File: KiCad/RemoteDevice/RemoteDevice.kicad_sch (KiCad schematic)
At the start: 56 parts, among them J1 pin, J2 pin, Q1 PJA3411, Q2 PJA3411, SW1 BP, SW2 BP, U1 XC9140, U10 XBEE-3, U2 STM32L041F6Px, U3 MCP6281, U4 ADT7410TRZ, U5 MCP6281, U6 RT606, U7 Microphone, U8 LD2981CU33, U9 Con_4pts

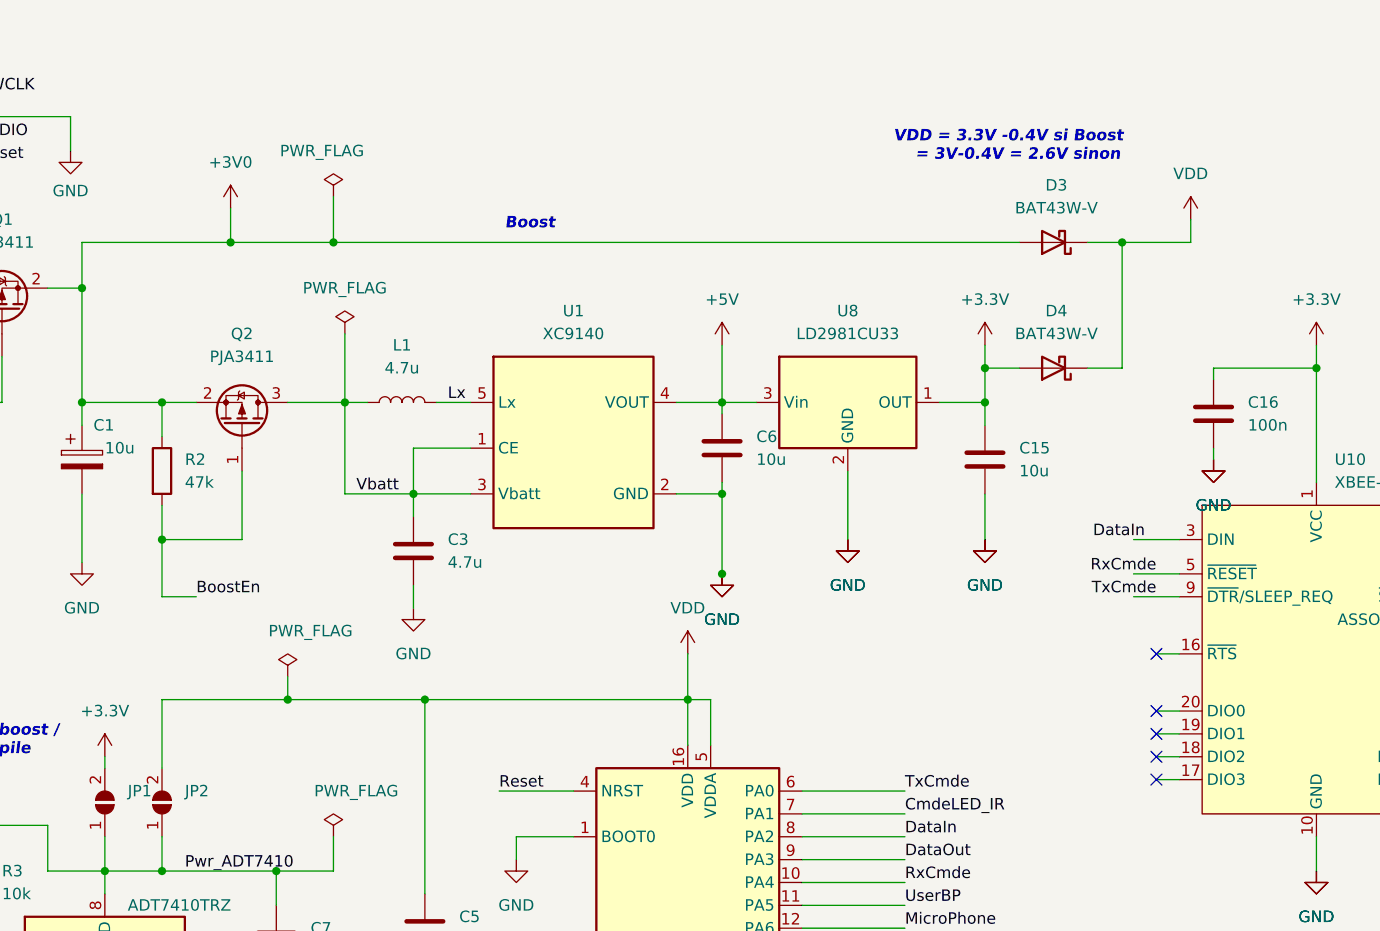
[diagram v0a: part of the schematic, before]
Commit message: Version modifié : ajout pull up RT606 pour adapt niveau, supression BAT43, ajout capa de découplage uC. A tester
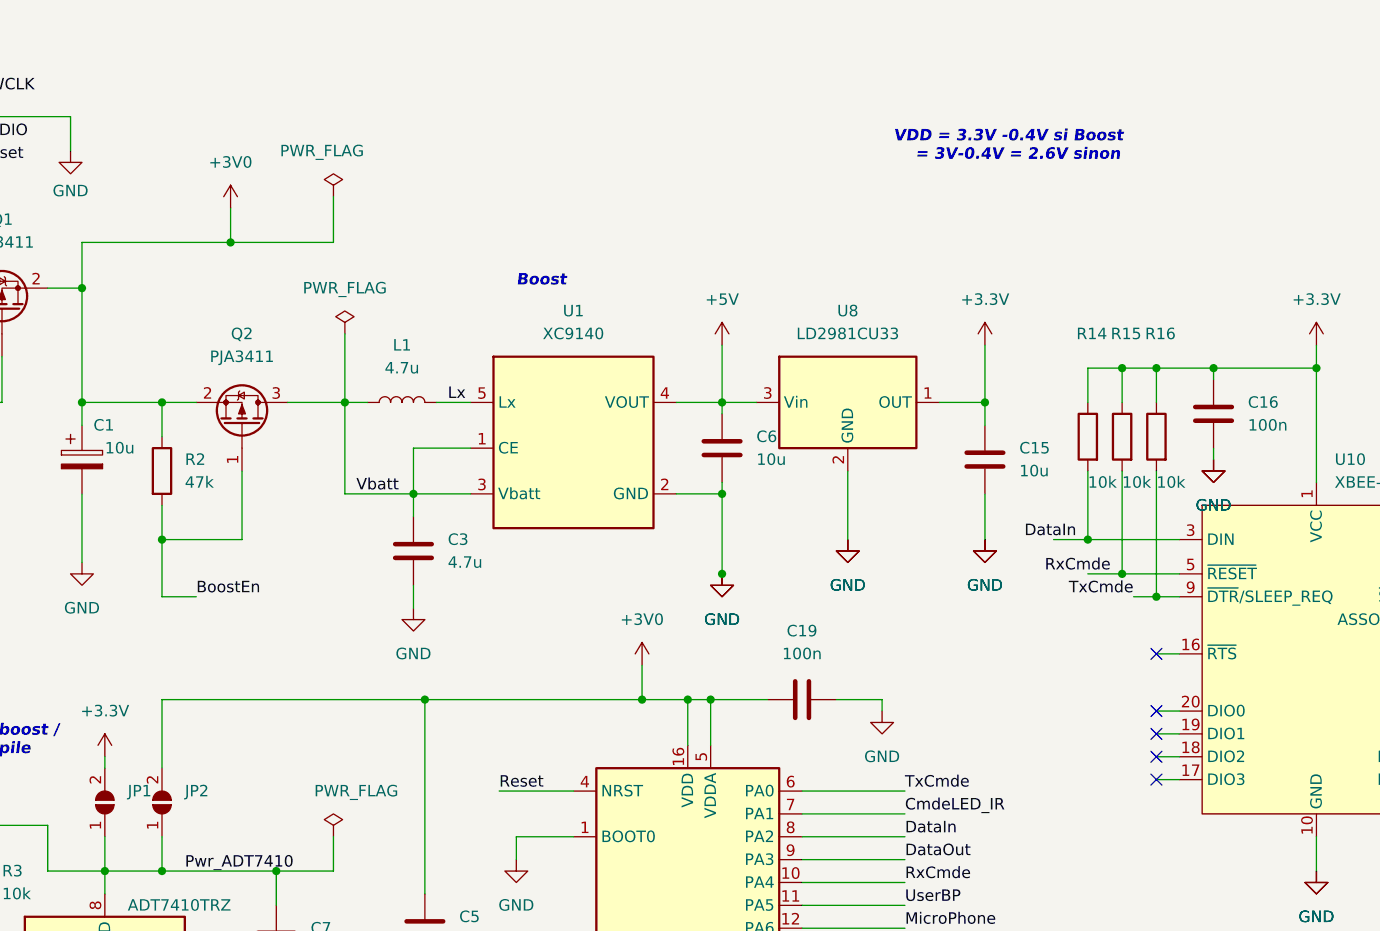
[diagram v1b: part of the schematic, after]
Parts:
- removed D3, D4: BAT43W-V, Diode_SMD:D_SOD-123, symbol Diode:BAT43W-V
- added C19: 100n, Capacitor_SMD:C_1206_3216Metric, symbol Device:C
- added R14, R15, R16: 10k, Resistor_SMD:R_1206_3216Metric, symbol Device:R
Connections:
- net VDD is gone; now on net +3V0: C5.1, JP2.2 (B), U2.16 (VDD), U2.5 (VDDA)
- net +3V0: now also C19.1
- net +3V3: now also R14.1, R15.1, R16.1
- net DataIn: now also R14.2
- net GND: now also C19.2
- net RxCmde: now also R15.2
- net TxCmde: now also R16.2
